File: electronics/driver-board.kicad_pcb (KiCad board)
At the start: 2 copper layers, 40 x 40 mm, 50 parts, among them J3 S4B-XH-A, J4 Qwiic_RA, J5 Conn_01x06_Female, J7 Conn_01x02, J8 Conn_01x08_Socket, J9 Conn_01x01_Socket, SW1 SW_Push, SW2 SW_Push, SW3 SW_Push, SW4 SW_Push, U1 LMR16006YQ3, U3 ESP32-C6-MINI-1/U, U5 TMC5240-TSSOP38, U7 AS5047D

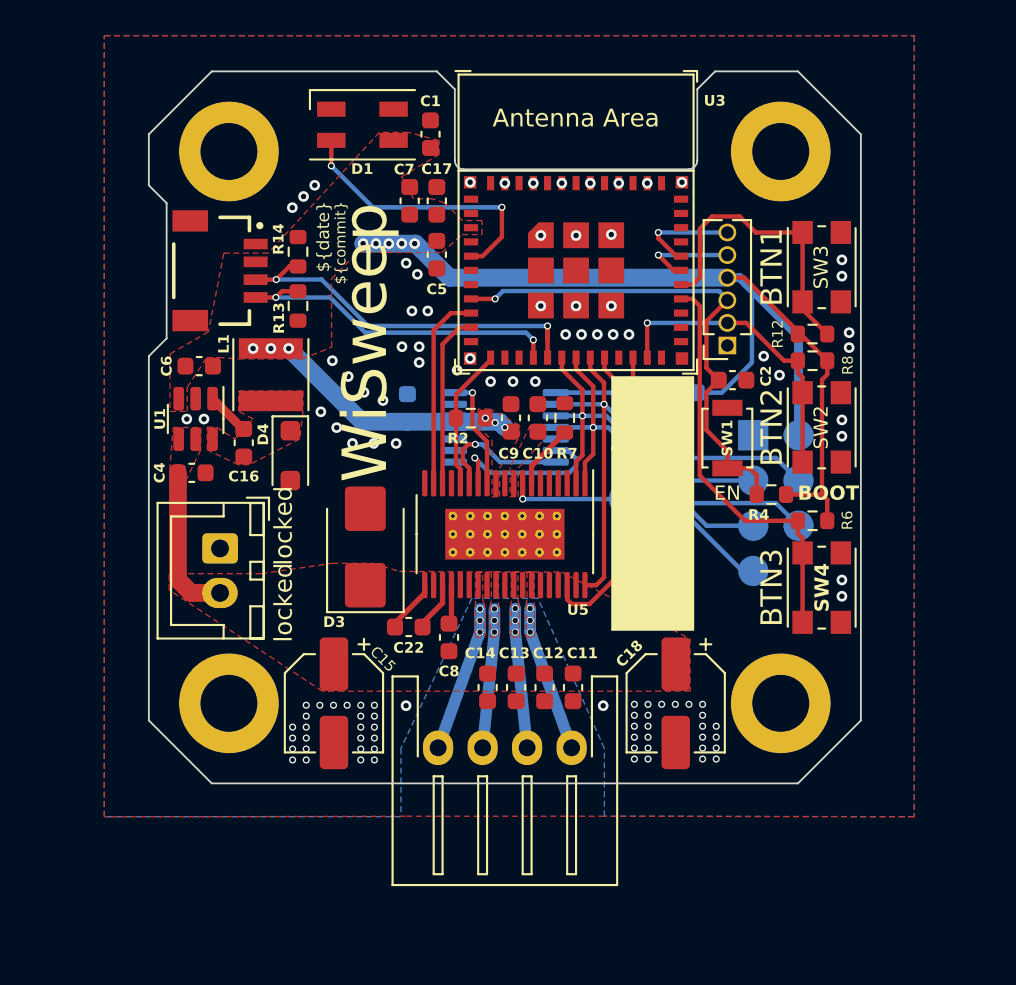
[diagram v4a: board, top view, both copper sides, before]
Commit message: incorporated USB port and refined board layout wip
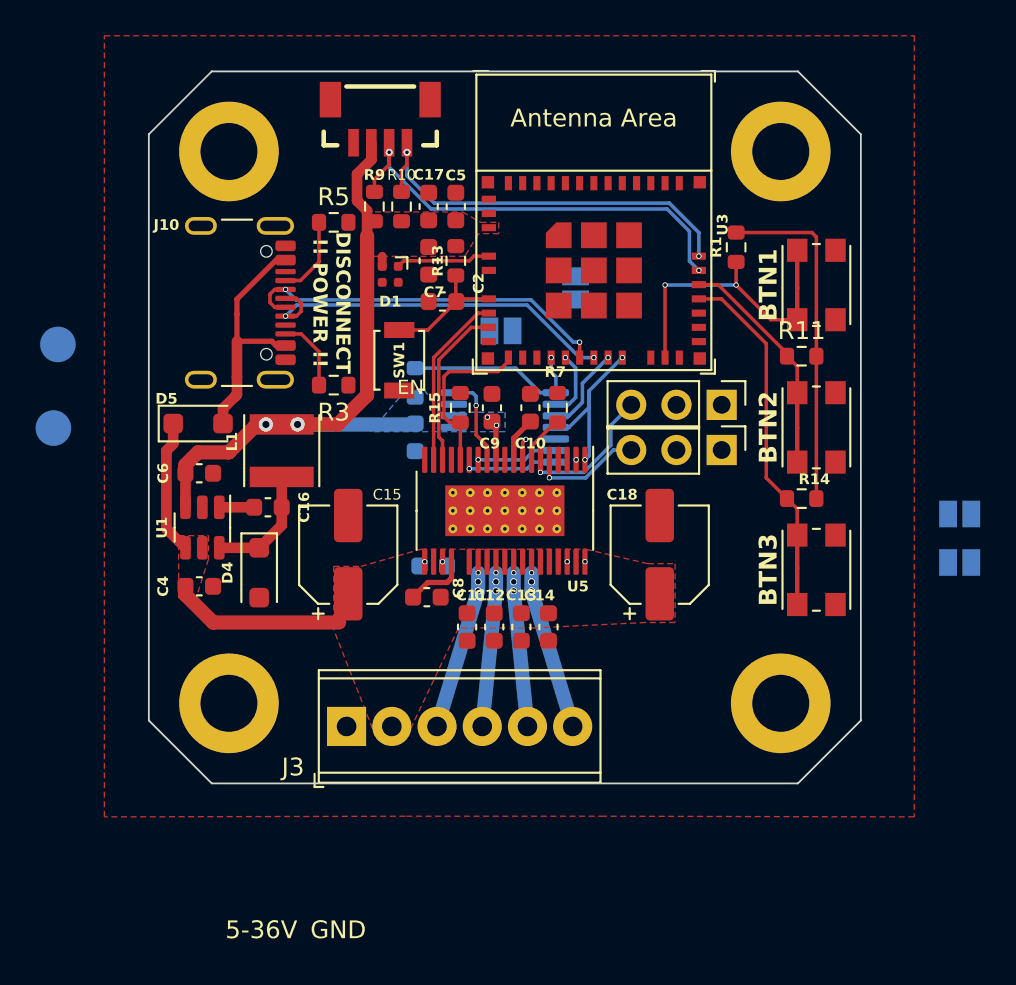
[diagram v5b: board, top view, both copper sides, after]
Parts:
- removed C1: 100nF, Capacitor_SMD:C_0603_1608Metric
- removed D3: SMB24A, Diode_SMD:D_SMB
- removed J5: Conn_01x06_Female, Connector_PinSocket_1.27mm:PinSocket_1x06_P1.27mm_Vertical
- removed J7: Conn_01x02, Connector_JST:JST_XH_B2B-XH-A_1x02_P2.50mm_Vertical
- removed J8: Conn_01x08_Socket, Connector_PinHeader_2.54mm:PinHeader_2x04_P2.54mm_Vertical
- removed R12, R4, R6, R8: 10k, Resistor_SMD:R_0603_1608Metric
- added D5: DS210W, Diode_SMD:D_SOD-123F, F.Cu at (32.8, 49.8)
- added J1: Conn_01x01_Socket, TestPoint:TestPoint_Pad_D2.0mm, B.Cu at (24.9, 45.3)
- added J10: USB_C_Receptacle_USB2.0, Connector_USB:USB_C_Receptacle_GCT_USB4105-xx-A_16P_TopMnt_Horizontal, F.Cu at (34.0, 43.0)
- added J2: Conn_01x03_Pin, Connector_PinHeader_2.54mm:PinHeader_1x03_P2.54mm_Vertical, F.Cu at (62.2, 51.3)
- added J6: Conn_01x03_Pin, Connector_PinHeader_2.54mm:PinHeader_1x03_P2.54mm_Vertical, F.Cu at (62.2, 48.7)
- added JP1: Jumper_2_Open, Jumper:SolderJumper-2_P1.3mm_Open_Pad1.0x1.5mm, B.Cu at (49.8, 44.6)
- added JP2: Jumper_2_Open, Jumper:SolderJumper-2_P1.3mm_Open_Pad1.0x1.5mm, B.Cu at (54.0, 42.2)
- added JP3: Jumper_2_Open, Jumper:SolderJumper-2_P1.3mm_Open_Pad1.0x1.5mm, B.Cu at (75.5, 57.6)
- added JP4: Jumper_2_Open, Jumper:SolderJumper-2_P1.3mm_Open_Pad1.0x1.5mm, B.Cu at (75.5, 54.9)
- added R10: 10k, Resistor_SMD:R_0603_1608Metric, F.Cu at (44.2, 37.6)
- added R11: 10k, Resistor_SMD:R_0603_1608Metric, F.Cu at (66.7, 46.0)
- added R15: 10k, Resistor_SMD:R_0603_1608Metric, F.Cu at (47.5, 48.9)
- added R3: 5k1, Resistor_SMD:R_0603_1608Metric, F.Cu at (40.4, 47.6)
- added R5: 5k1, Resistor_SMD:R_0603_1608Metric, F.Cu at (40.4, 38.5)
- added R9: 10k, Resistor_SMD:R_0603_1608Metric, F.Cu at (42.7, 37.6)
- C22, R2: moved to B.Cu
- D1: footprint LED_SMD:LED_SK6812MINI_PLCC4_3.5x3.5mm_P1.75mm -> LED_SMD:LED_SK6812_EC15_1.5x1.5mm
- J3: value S4B-XH-A -> Conn_01x06; footprint Connector_JST:JST_XH_S4B-XH-A-1_1x04_P2.50mm_Horizontal -> TerminalBlock_Phoenix:TerminalBlock_Phoenix_MPT-0,5-6-2.54_1x06_P2.54mm_Horizontal
- J4: footprint SparkFun-Connector:JST04_1MM_RA -> SparkFun-Connector:JST04_1MM_Vertical
- R1: moved to F.Cu
- moved J9 32.5 mm to (24.6, 50.0)
- moved R14 31.5 mm to (66.7, 54.0), turned to 0 degrees
- moved SW1 18.9 mm to (44.1, 46.2), turned to -90 degrees
- moved C2 16.9 mm to (46.5, 42.9), turned to 180 degrees
- moved J4 11.2 mm to (43.0, 32.5), turned to 0 degrees
- moved R13 9.22 mm to (47.2, 40.6), turned to 90 degrees
- moved SW3 9.00 mm to (67.5, 50.0)
- moved R1 8.70 mm to (63.0, 39.9), turned to 90 degrees
- moved D1 8.55 mm to (43.6, 41.4), turned to -90 degrees
- moved C18 8.40 mm to (58.7, 57.1), turned to 90 degrees
- moved C15 8.39 mm to (41.2, 57.1), turned to 90 degrees
- moved SW2 8.01 mm to (67.5, 42.0)
- moved C11 6.85 mm to (47.9, 61.2)
- moved D4 6.80 mm to (36.2, 58.2)
- moved C4 6.39 mm to (32.8, 58.9)
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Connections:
- net /ENCA renamed /AS_ENCA
- net /ENCB renamed /AS_ENCB
- net /ENCN renamed /AS_ENCN
- net /SW_BTN1 renamed /BTN2
- net /TMC_DIAG0 renamed /ESP_GPIO5
- net /TMC_DIAG1 renamed /ESP_GPIO4
- net Net-(D1-DIN) renamed /ESP_GPIO2
- net Net-(J9-Pin_1) renamed /TMC_AIN
- C8 pad 1: Net-(U5-VCP) -> VBUS
- C8 pad 2: VBUS -> Net-(U5-VCP)
- J3 pad 1: /TMC_OUT1B -> GND
- J3 pad 2: /TMC_OUT2B -> VBUS
- J3 pad 3: /TMC_OUT2A -> /TMC_OUT1B
- J3 pad 4: /TMC_OUT1A -> /TMC_OUT2B
- J4 pad 3: /I2C_SDA -> /ESP_GPIO17
- J4 pad 4: /I2C_SCL -> /ESP_GPIO16
- R1 pad 1: /SPI_CSN_ENC -> /BTN1
- R13 pad 1: /I2C_SCL -> /ESP_EN
- R14 pad 1: /I2C_SDA -> /BTN3
- R2 pad 1: +3V3 -> /AS_SPI_CSN
- R2 pad 2: /TMC_ENABLE -> +3V3
- R7 pad 1: GND -> Net-(U5-IREF)
- R7 pad 2: Net-(U5-IREF) -> GND
- SW2 pad 2: /ESP_BOOT -> /BTN1
- SW4 pad 2: /SW_BTN3 -> /BTN3
- U3 pad 12: /TMC_ENABLE -> /ESP_GPIO0
- U3 pad 13: unconnected-(U3-GPIO1/ADC1_CH1/XTAL_32K_N-Pad13) -> /ESP_GPIO1
- U3 pad 15: /I2C_SCL -> /AS_SPI_CSN
- U3 pad 16: /I2C_SDA -> /AS_CLK
- U3 pad 17: /SPI_SDO -> /ESP_GPIO12
- U3 pad 18: /SPI_SDI -> /ESP_GPIO13
- U3 pad 19: /SPI_SCK -> /AS_MISO
- U3 pad 20: /SPI_CSN_TMC -> /AS_MOSI
- U3 pad 22: /SPI_CSN_ENC -> /ESP_GPIO8
- U3 pad 23: /ESP_BOOT -> /BTN1
- U3 pad 24: unconnected-(U3-GPIO18-Pad24) -> /ESP_GPIO18
- U3 pad 25: unconnected-(U3-GPIO19-Pad25) -> /ESP_GPIO19
- U3 pad 26: unconnected-(U3-GPIO20-Pad26) -> /ESP_GPIO20
- U3 pad 27: unconnected-(U3-GPIO21-Pad27) -> /ESP_GPIO21
- U3 pad 28: /SW_BTN3 -> /BTN3
- U3 pad 30: /ESP_UART_RXD -> /ESP_GPIO17
- U3 pad 31: /ESP_UART_TXD -> /ESP_GPIO16
- U3 pad 6: unconnected-(U3-GPIO3/ADC1_CH3-Pad6) -> /ESP_GPIO3
- U5 pad 1: /SPI_SDI -> /AS_MOSI
- U5 pad 15: /TMC_ENABLE -> /ESP_GPIO0
- U5 pad 19: unconnected-(U5-OV-Pad19) -> /TMC_OV
- U5 pad 2: /SPI_SDO -> /AS_MISO
- U5 pad 21: (no net) -> GND
- U5 pad 34: (no net) -> GND
- U5 pad 36: /SPI_CSN_TMC -> /ESP_GPIO8
- U5 pad 37: (no net) -> GND
- U5 pad 38: /SPI_SCK -> /AS_CLK
- U5 pad 4: (no net) -> GND
- U5 pad 5: unconnected-(U5-REFL-Pad5) -> /TMC_REFL
- U5 pad 6: unconnected-(U5-REFR-Pad6) -> /TMC_REFR
- U7 pad 1: /SPI_CSN_ENC -> /AS_SPI_CSN
- U7 pad 2: /SPI_SCK -> /AS_CLK
- U7 pad 3: /SPI_SDO -> /AS_MISO
- U7 pad 4: /SPI_SDI -> /AS_MOSI
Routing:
- net /SPI_CSN_TMC: track 27.5 -> 0.00 mm, vias 1 -> 0
- net /SPI_SCK: track 26.9 -> 0.00 mm, vias 1 -> 0
- net /ESP_GPIO17: track 0.00 -> 24.9 mm, vias 0 -> 2
- net /SPI_SDO: track 24.1 -> 0.00 mm, vias 1 -> 0
- net /SW_BTN3: track 23.5 -> 0.00 mm
- net /ESP_GPIO16: track 0.00 -> 23.2 mm, vias 0 -> 2
- net /I2C_SDA: track 21.6 -> 0.00 mm, vias 2 -> 0
- net /ESP_EN: track 28.7 -> 7.23 mm, vias 1 -> 0
- net /SPI_SDI: track 21.5 -> 0.00 mm, vias 1 -> 0
- net /ESP_GPIO13: track 0.00 -> 21.2 mm, vias 0 -> 2
- net /ESP_GPIO12: track 0.00 -> 21.1 mm, vias 0 -> 2
- net /SPI_CSN_ENC: track 20.6 -> 0.00 mm, vias 1 -> 0
- net /BTN3: track 0.00 -> 20.2 mm
- net /I2C_SCL: track 19.0 -> 0.00 mm, vias 2 -> 0
- net /BTN1: track 0.00 -> 17.5 mm, vias 0 -> 2
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- added copper zone on B.Cu, net +3V3
- removed copper zone on F.Cu, net /TMC_OUT1A
- removed copper zone on F.Cu, net /TMC_OUT1B
- removed copper zone on F.Cu, net /TMC_OUT2A
- removed copper zone on F.Cu, net /TMC_OUT2B
- removed copper zone on B.Cu, net GND
- removed copper zone on F.Cu, net Net-(D4-K)
- removed copper zone on F.Cu, net Net-(U5-VDD1V8)
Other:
- outline, holes or cut-outs redrawn
- copper layers 2 -> 4
- board text added: "5-36V"
- board text added: "DISCONNECT !! POWER !!"
- board text added: "GND"
- board text removed: "BOOT"
- board text removed: "GND BOOT EN 3v3 RXD TXD"
- board text removed: "locked"

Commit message: wip 4-layer layout
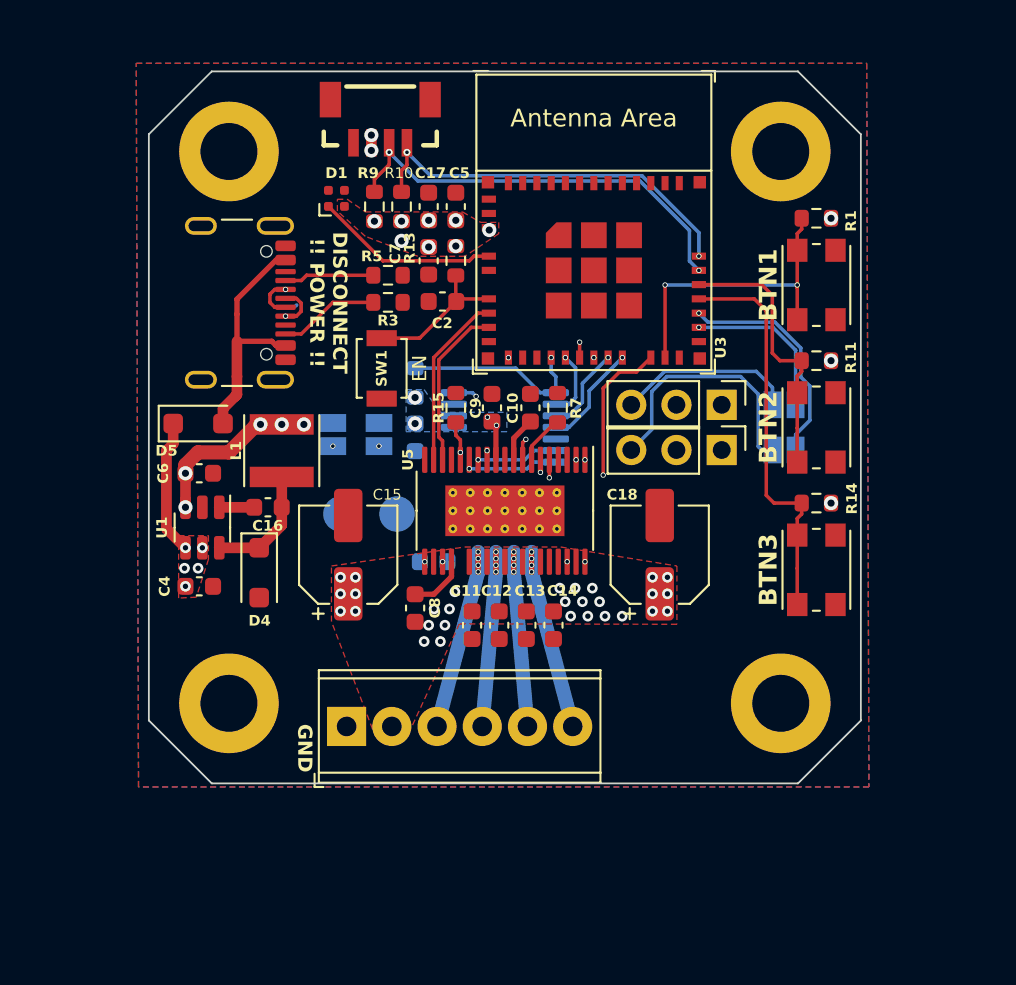
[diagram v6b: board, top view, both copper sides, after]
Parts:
- moved J9 19.9 mm to (43.9, 54.9), turned to 0 degrees
- moved J1 18.5 mm to (40.8, 54.9), turned to 0 degrees
- moved JP2 13.8 mm to (42.9, 50.4)
- moved JP3 11.7 mm to (65.7, 51.3)
- moved JP4 11.6 mm to (65.7, 48.7)
- moved JP1 11.1 mm to (40.3, 50.4), turned to 90 degrees
- moved R3 5.56 mm to (43.4, 43.0)
- moved D1 5.23 mm to (40.5, 37.1), turned to 90 degrees
- moved R1 4.79 mm to (67.5, 38.3), turned to 0 degrees
- moved R5 4.26 mm to (43.4, 41.5)
- moved SW1 1.09 mm to (43.1, 46.7)
- moved C8 0.90 mm to (45.0, 60.1), turned to 90 degrees
- moved R11 0.86 mm to (67.5, 46.3)
- moved R14 0.86 mm to (67.5, 54.3)
- moved C11 0.30 mm to (48.2, 61.1)
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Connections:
- JP3 pad 1: /ESP_GPIO20 -> /ESP_GPIO21
- JP4 pad 2: /ESP_GPIO21 -> /ESP_GPIO20
- U5 pad 21: GND -> (no net)
- U5 pad 34: GND -> (no net)
- U5 pad 37: GND -> (no net)
- U5 pad 4: GND -> (no net)
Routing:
- net +3V3: track 60.5 -> 12.1 mm, vias 4 -> 22
- net /TMC_REFL: track 6.26 -> 20.6 mm
- net /ESP_GPIO8: track 0.00 -> 14.0 mm, vias 1 -> 2
- net /ESP_GPIO21: track 0.00 -> 12.8 mm, vias 0 -> 1
- net /TMC_REFR: track 8.04 -> 18.1 mm
- net VBUS: track 17.2 -> 7.45 mm, vias 0 -> 34
- net /ESP_GPIO20: track 0.00 -> 9.04 mm, vias 0 -> 1
- net /AS_ENCA: track 5.02 -> 13.2 mm, vias 1 -> 2
- net /AS_MISO: track 4.92 -> 11.4 mm
- net /AS_ENCB: track 4.58 -> 10.5 mm, vias 1 -> 2
- net /ESP_GPIO2: track 5.33 -> 10.4 mm
- net /AS_MOSI: track 10.4 -> 13.8 mm
- net /BTN2: track 12.9 -> 15.3 mm
- net /BTN3: track 20.2 -> 22.4 mm
- net /USB_CC2: track 4.17 -> 5.66 mm
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- added copper zone on In1.Cu, net +3V3
- added copper zone on B.Cu, net GND
- added copper zone on In1.Cu, net VBUS
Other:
- board text added: "+"
- board text added: "-"
- board text added: "github.com/slimcdk/wisweep ${date} @ ${commit}"
- board text removed: "${date} @ ${commit}"
- board text removed: "github.com/slimcdk/wisweep"

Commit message: more routing
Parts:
- removed J2, J6: Conn_01x03_Pin, Connector_PinHeader_2.54mm:PinHeader_1x03_P2.54mm_Vertical
- added J5: Conn_02x03_Counter_Clockwise, Connector_PinHeader_2.54mm:PinHeader_2x03_P2.54mm_Vertical, F.Cu at (62.2, 48.7)
- moved J1 23.0 mm to (60.5, 66.9)
- moved J9 17.9 mm to (57.2, 66.9)
- moved R1 16.0 mm to (67.5, 54.3)
- moved R14 16.0 mm to (67.5, 38.3)
- moved SW2 16.0 mm to (67.5, 58.0)
- moved SW4 16.0 mm to (67.5, 42.0)
- moved JP4 7.21 mm to (61.3, 54.4), turned to 90 degrees
- moved JP3 3.67 mm to (63.8, 54.4), turned to -90 degrees
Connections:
- net /AS_CLK renamed /ESP_GPIO7
- net /AS_MISO renamed /ESP_GPIO14
- net /AS_SPI_CSN renamed /ESP_GPIO6
- JP2 pad 2: /AS_MOSI -> /ESP_GPIO3
- U3 pad 20: /AS_MOSI -> /ESP_GPIO15
- U3 pad 28: /BTN3 -> /BTN2
- U3 pad 29: /BTN2 -> /BTN3
- U5 pad 1: /AS_MOSI -> /ESP_GPIO15
- U7 pad 4: /AS_MOSI -> /ESP_GPIO15
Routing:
- net /TMC_REFL: track 20.6 -> 6.24 mm
- net /AS_MOSI: track 13.8 -> 0.00 mm, vias 2 -> 0
- net /ESP_GPIO21: track 12.8 -> 0.00 mm
- net /ESP_GPIO7: track 3.75 -> 15.7 mm
- net /TMC_OUT1B: track 10.1 -> 20.2 mm
- net /TMC_OUT1A: track 10.1 -> 20.2 mm
- net /TMC_REFR: track 18.1 -> 8.02 mm
- net /TMC_OUT2B: track 9.84 -> 19.7 mm
- net /TMC_OUT2A: track 9.84 -> 19.7 mm
- net /ESP_GPIO15: track 0.00 -> 9.81 mm, vias 0 -> 2
- net /BTN3: track 22.4 -> 12.6 mm, vias 0 -> 2
- net /ESP_GPIO20: track 9.04 -> 0.00 mm
- net /BTN1: track 17.3 -> 21.6 mm
- net /BTN2: track 15.3 -> 16.0 mm, vias 0 -> 2
- net /ESP_GPIO5: track 9.31 -> 8.58 mm, vias 0 -> 2
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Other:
- board text added: "${version}"
